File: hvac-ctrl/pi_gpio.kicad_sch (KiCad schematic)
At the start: 31 parts

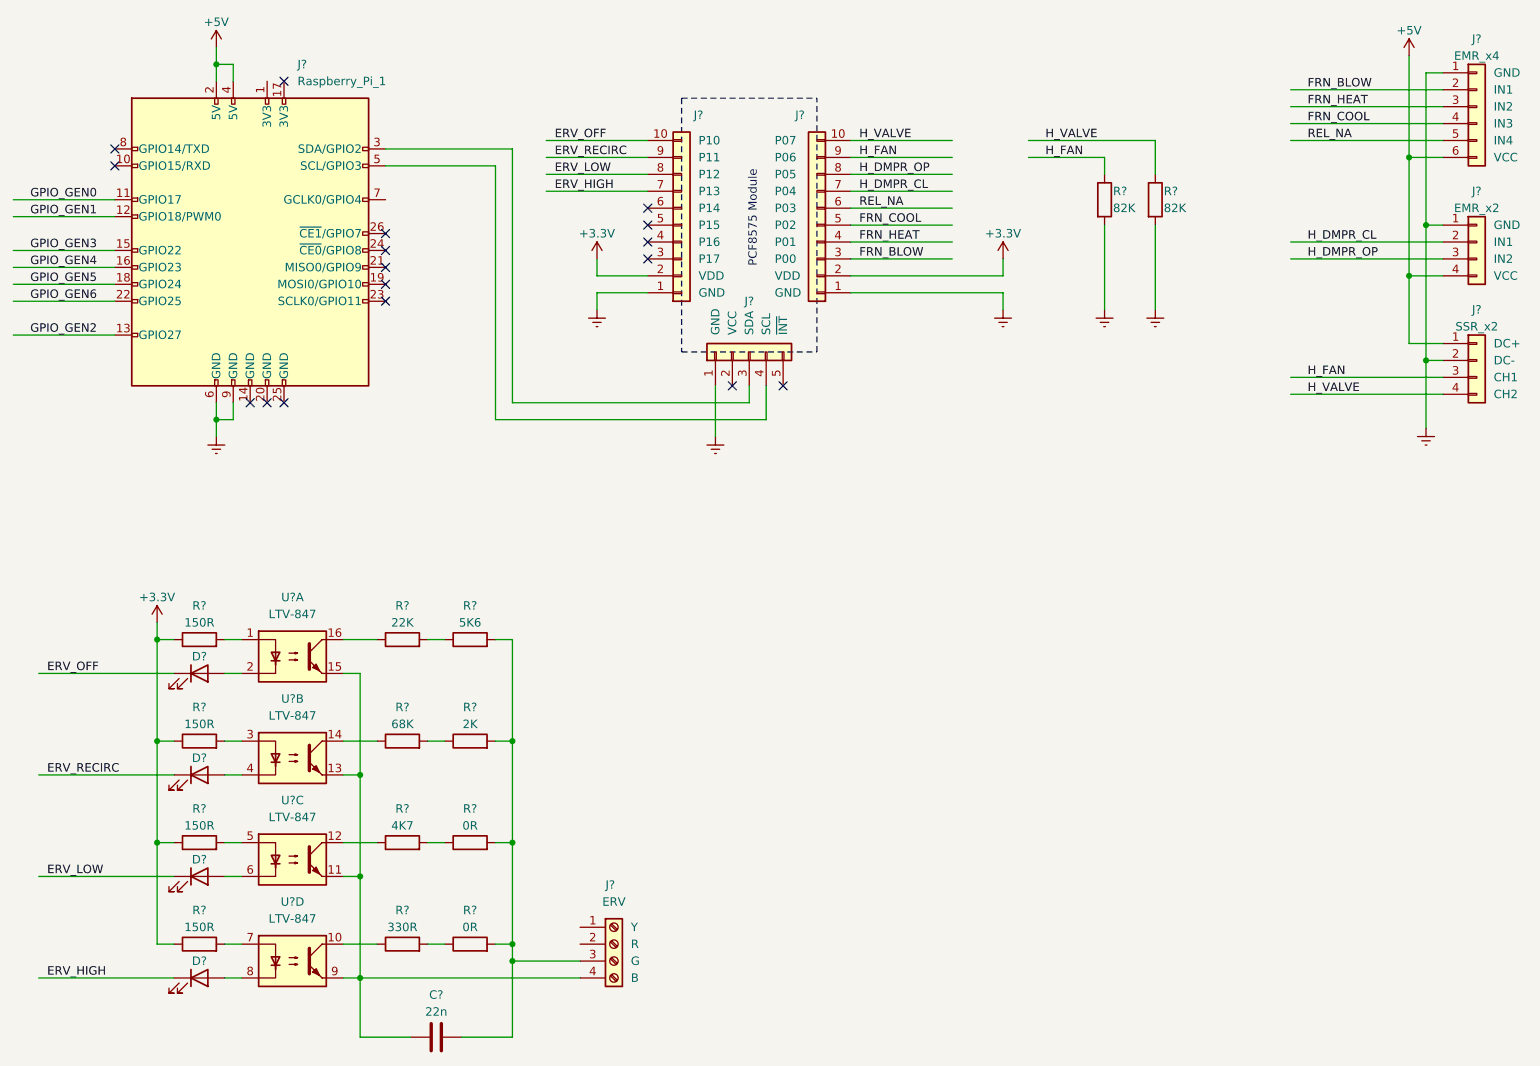
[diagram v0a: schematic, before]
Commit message: Add ERV data input circuit
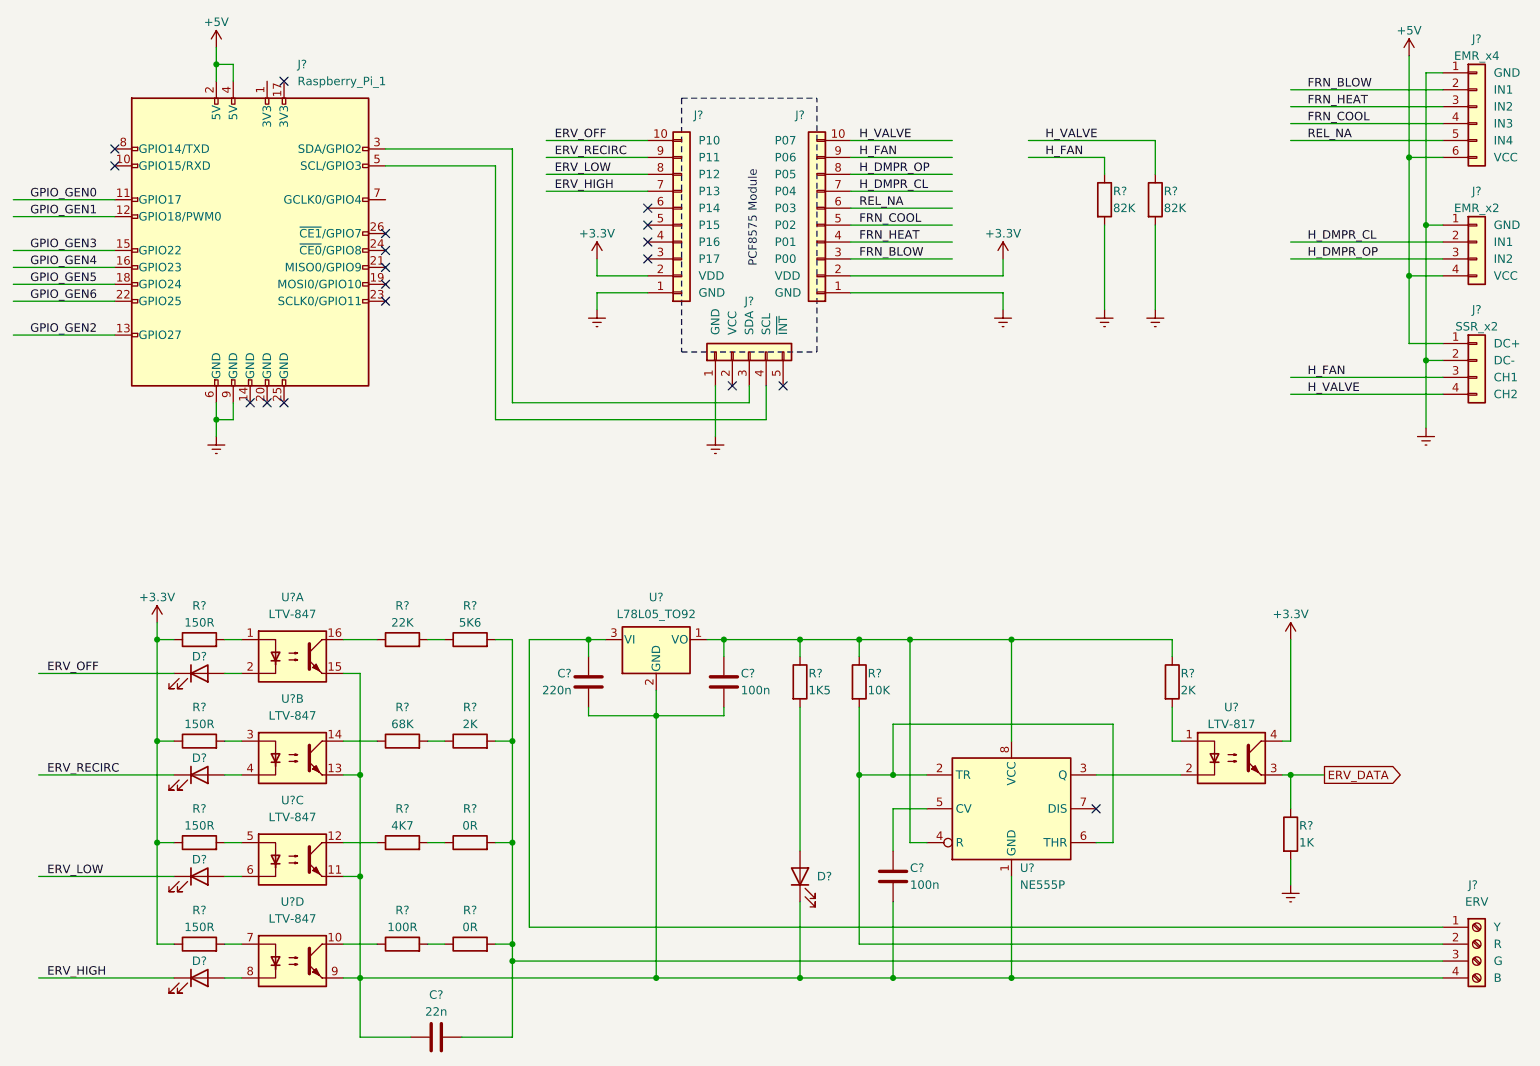
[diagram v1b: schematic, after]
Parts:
- added C? (x2): 100n, symbol Device:C
- added C?: 220n, symbol Device:C
- added D?: LED, symbol Device:LED
- added R?: 1K, symbol Device:R
- added R?: 2K, symbol Device:R
- added R?: 1K5, symbol Device:R
- added R?: 10K, symbol Device:R
- added U?: NE555P, Package_DIP:DIP-8_W7.62mm, symbol Timer:NE555P
- added U?: L78L05_TO92, Package_TO_SOT_THT:TO-92_Inline, symbol Regulator_Linear:L78L05_TO92
- added U?: LTV-817, Package_DIP:DIP-4_W7.62mm, symbol Isolator:LTV-817
- R?: value 330R -> 100R
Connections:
- net +3.3V: now also U?.4
- net Earth: now also R?.2
- net at C?.1, J?.4 (Pin_4), U?.11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: now also C?.2, C?.2, C?.2, D?.1 (K), U?.1 (GND), U?.2 (GND)
- net at J?.1 (Pin_1): now also C?.1, U?.3 (VI)
- net at J?.2 (Pin_2): now also R?.2, U?.2 (TR), U?.6 (THR)
- new net: U?.2, U?.3 (Q)
- new net: C?.1, R?.1, R?.1, R?.1, U?.1 (VO), U?.4 (R), U?.8 (VCC)
- new net: C?.1, U?.5 (CV)
- new net: D?.2 (A), R?.2
- new net: R?.2, U?.1
- new net ERV_DATA: R?.1, U?.3
- no-connect marks 17 -> 18
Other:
- moved on the sheet: J?

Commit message: Update schematic with the latest prototype improvements
- Change series resistor value on the ERV control optocoupler LED side
- Add ERV power monitor LED.
- Add resistive dividers for sensing the 5V and 18V rails voltage.
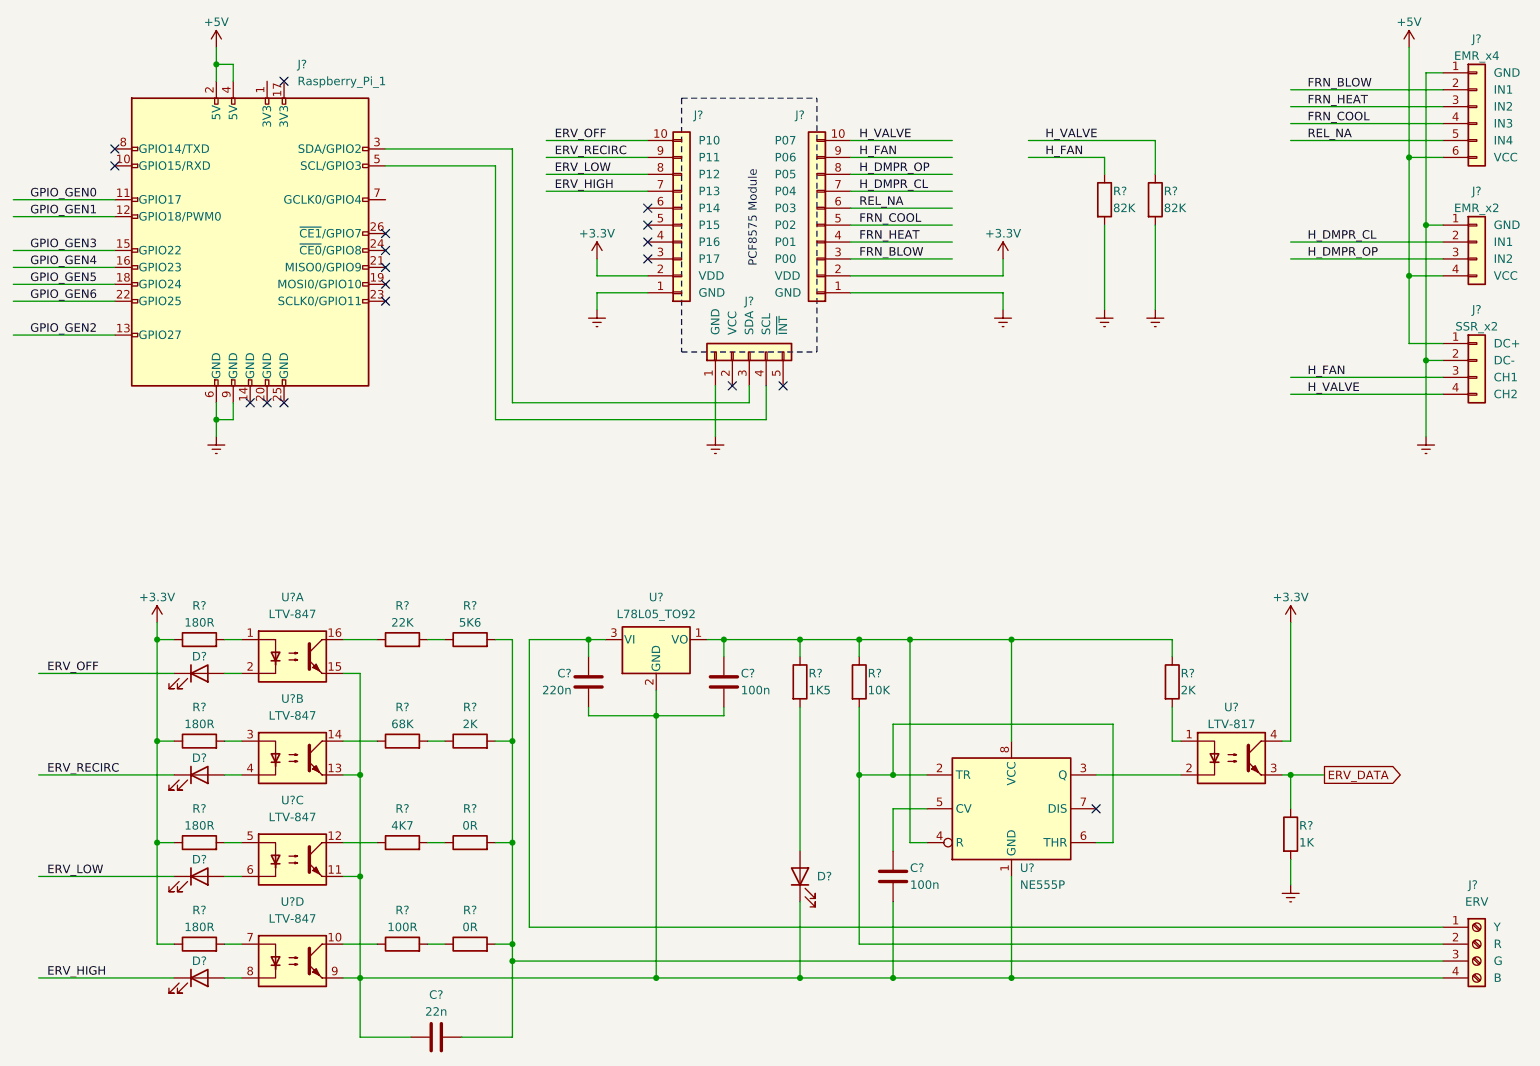
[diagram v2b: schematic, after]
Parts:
- R? (x4): value 150R -> 180R
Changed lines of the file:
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@@
     (stroke (width 0) (type default))
   )
-  (wire (pts (xy 214.63 113.03) (xy 214.63 128.27))
+  (wire (pts (xy 214.63 110.49) (xy 214.63 128.27))
     (stroke (width 0) (type default))
   )
@@
     (stroke (width 0) (type default))
   )
-  (wire (pts (xy 234.95 71.12) (xy 234.95 81.28))
+  (wire (pts (xy 234.95 71.12) (xy 234.95 82.55))
     (stroke (width 0) (type default))
   )
@@
     (stroke (width 0) (type default))
   )
-  (wire (pts (xy 232.41 40.64) (xy 232.41 25.4))
+  (wire (pts (xy 232.41 40.64) (xy 232.41 24.13))
     (stroke (width 0) (type default))
   )
@@
       (effects (font (size 1.27 1.27)))
     )
-    (property "Value" "150R" (at 50.8 110.49 90)
+    (property "Value" "180R" (at 50.8 110.49 90)
       (effects (font (size 1.27 1.27)))
     )
@@
       (effects (font (size 1.27 1.27)))
     )
-    (property "Value" "150R" (at 50.8 156.21 90)
+    (property "Value" "180R" (at 50.8 156.21 90)
       (effects (font (size 1.27 1.27)))
     )
@@
       (effects (font (size 1.27 1.27)))
     )
-    (property "Value" "150R" (at 50.8 140.97 90)
+    (property "Value" "180R" (at 50.8 140.97 90)
       (effects (font (size 1.27 1.27)))
     )
@@
       (effects (font (size 1.27 1.27)))
     )
-    (property "Value" "150R" (at 50.8 125.73 90)
+    (property "Value" "180R" (at 50.8 125.73 90)
       (effects (font (size 1.27 1.27)))
     )
@@
     )
   )
-  (symbol (lib_id "power:+5V") (at 232.41 25.4 0) (unit 1)
-    (in_bom yes) (on_board yes) (dnp no)
-    (property "Reference" "#PWR0120" (at 232.41 29.21 0)
-      (effects (font (size 1.27 1.27)) hide)
-    )
-    (property "Value" "+5V" (at 232.41 21.59 0)
-      (effects (font (size 1.27 1.27)))
-    )
-    (property "Footprint" "" (at 232.41 25.4 0)
-      (effects (font (size 1.27 1.27)) hide)
-    )
-    (property "Datasheet" "" (at 232.41 25.4 0)
+  (symbol (lib_id "power:+5V") (at 232.41 24.13 0) (unit 1)
+    (in_bom yes) (on_board yes) (dnp no)
+    (property "Reference" "#PWR0120" (at 232.41 27.94 0)
+      (effects (font (size 1.27 1.27)) hide)
+    )
+    (property "Value" "+5V" (at 232.41 20.32 0)
+      (effects (font (size 1.27 1.27)))
+    )
+    (property "Footprint" "" (at 232.41 24.13 0)
+      (effects (font (size 1.27 1.27)) hide)
+    )
+    (property "Datasheet" "" (at 232.41 24.13 0)
       (effects (font (size 1.27 1.27)) hide)
     )
@@
     )
   )
-  (symbol (lib_id "power:+3.3V") (at 214.63 113.03 0) (unit 1)
-    (in_bom yes) (on_board yes) (dnp no)
-    (property "Reference" "#PWR02" (at 214.63 116.84 0)
-      (effects (font (size 1.27 1.27)) hide)
-    )
-    (property "Value" "+3.3V" (at 214.63 109.22 0)
-      (effects (font (size 1.27 1.27)))
-    )
-    (property "Footprint" "" (at 214.63 113.03 0)
-      (effects (font (size 1.27 1.27)) hide)
-    )
-    (property "Datasheet" "" (at 214.63 113.03 0)
+  (symbol (lib_id "power:+3.3V") (at 214.63 110.49 0) (unit 1)
+    (in_bom yes) (on_board yes) (dnp no)
+    (property "Reference" "#PWR02" (at 214.63 114.3 0)
+      (effects (font (size 1.27 1.27)) hide)
+    )
+    (property "Value" "+3.3V" (at 214.63 106.68 0)
+      (effects (font (size 1.27 1.27)))
+    )
+    (property "Footprint" "" (at 214.63 110.49 0)
+      (effects (font (size 1.27 1.27)) hide)
+    )
+    (property "Datasheet" "" (at 214.63 110.49 0)
       (effects (font (size 1.27 1.27)) hide)
     )
@@
     )
   )
-  (symbol (lib_id "power:Earth") (at 234.95 81.28 0) (unit 1)
+  (symbol (lib_id "power:Earth") (at 234.95 82.55 0) (unit 1)
     (in_bom yes) (on_board yes) (dnp no) (fields_autoplaced)
-    (property "Reference" "#PWR0121" (at 234.95 87.63 0)
-      (effects (font (size 1.27 1.27)) hide)
-    )
-    (property "Value" "Earth" (at 234.95 85.09 0)
-      (effects (font (size 1.27 1.27)) hide)
-    )
-    (property "Footprint" "" (at 234.95 81.28 0)
-      (effects (font (size 1.27 1.27)) hide)
-    )
-    (property "Datasheet" "~" (at 234.95 81.28 0)
-      (effects (font (size 1.27 1.27)) hide)
-    )
+    (property "Reference" "#PWR0121" (at 234.95 88.9 0)
+      (effects (font (size 1.27 1.27)) hide)
+    )
+    (property "Value" "Earth" (at 234.95 86.36 0)
+      (effects (font (size 1.27 1.27)) hide)
+    )
+    (property "Footprint" "" (at 234.95 82.55 0)
+      (effects (font (size 1.27 1.27)) hide)
+    )
+    (property "Datasheet" "~" (at 234.95 82.55 0)
+      (effects (font (size 1.27 1.27)) hide)
+    )
